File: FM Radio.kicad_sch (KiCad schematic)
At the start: 39 parts, among them IC1 SI4831-B30-GUR, J2 Conn_01x02_Pin, J4 CONSMA020.062-G, J6 CONSMA020.062-G, SW1 SW_SPDT, SW2 SW_DIP_x01, SW3 SW_Push, SW4 SW_Push, U3 LM1117MP-3.3, Y1 ECS-.327-12.5-34B-TR

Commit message: Add comments and fix errors
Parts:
- removed SW3, SW4: SW_Push, FM Radio:D6R40F1LFS, symbol Switch:SW_Push
- added S1, S2: D6R50F1LFS, D6R40F1LFS, symbol D6R50F1LFS:D6R50F1LFS
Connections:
- net GND: now also L1.1, S1.3 (NO_1), S1.4 (NO_2), S2.3 (NO_1), S2.4 (NO_2)
- net at IC1.17 (VOL-/BASS), R9.2: now also S1.1 (COM_1), S1.2 (COM_2)
- net at IC1.16 (VOL+/TREBLE), R10.2: now also S2.1 (COM_1), S2.2 (COM_2)
- net at IC1.8 (FMI), L1.2: now also C16.1
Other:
- moved on the sheet: C16, C8, C9, D3, L1, R11, U3

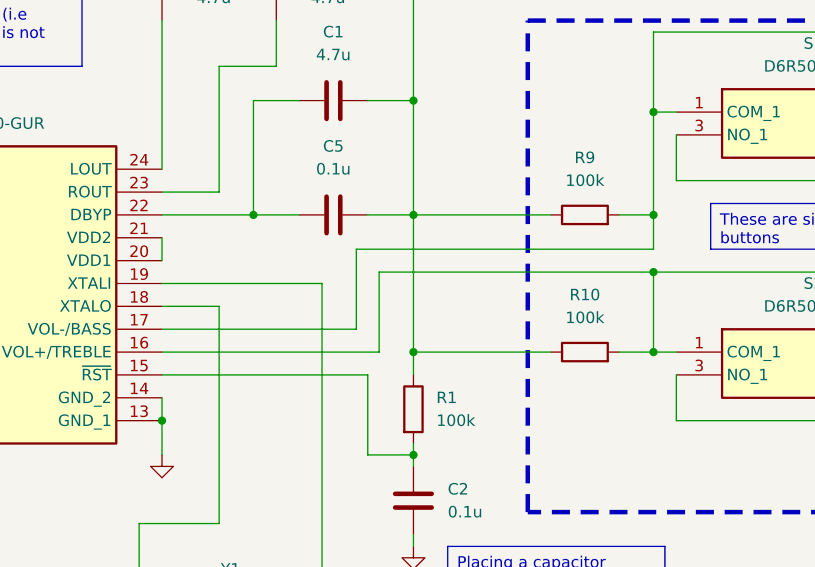
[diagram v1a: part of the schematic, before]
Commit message: Fix: VDD not connected
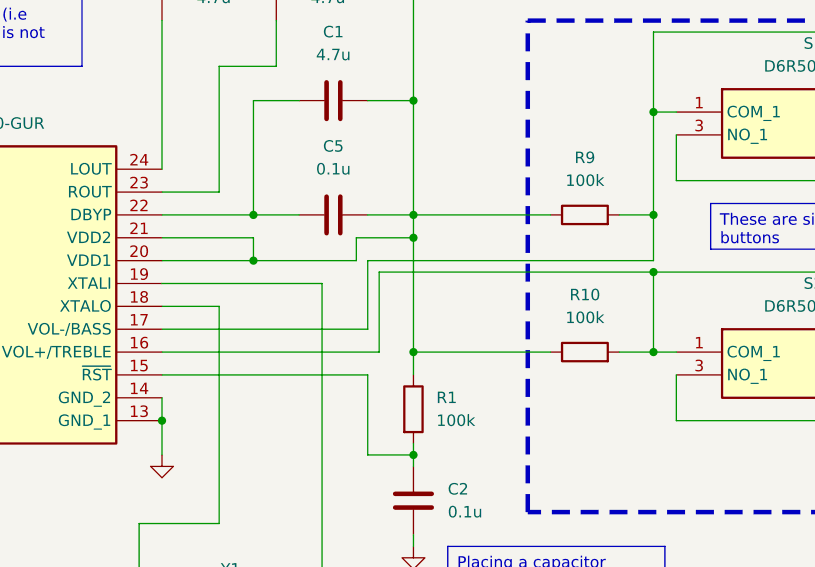
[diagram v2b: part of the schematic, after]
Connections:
- net +3.3V: now also IC1.20 (VDD1), IC1.21 (VDD2)
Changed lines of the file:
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@@
 (kicad_sch (version 20230121) (generator eeschema)
   (paper "A4")
+  (junction (at 215.9 99.06) (diameter 0) (color 0 0 0 0)
+  )
   (junction (at 57.15 156.21) (diameter 0) (color 0 0 0 0)
   )
@@
   (junction (at 138.43 91.44) (diameter 0) (color 0 0 0 0)
   )
+  (junction (at 242.57 102.87) (diameter 0) (color 0 0 0 0)
+  )
   (junction (at 275.59 92.71) (diameter 0) (color 0 0 0 0)
   )
@@
   (junction (at 242.57 85.09) (diameter 0) (color 0 0 0 0)
   )
-  (junction (at 242.57 102.87) (diameter 0) (color 0 0 0 0)
-  )
   (junction (at 36.83 167.64) (diameter 0) (color 0 0 0 0)
   )
   (junction (at 242.57 111.76) (diameter 0) (color 0 0 0 0)
+  )
+  (junction (at 198.12 101.6) (diameter 0) (color 0 0 0 0)
   )
   (junction (at 215.9 111.76) (diameter 0) (color 0 0 0 0)
@@
     (stroke (width 0) (type default))
   )
+  (wire (pts (xy 215.9 99.06) (xy 215.9 111.76))
+    (stroke (width 0) (type default))
+  )
   (wire (pts (xy 242.57 76.2) (xy 242.57 85.09))
     (stroke (width 0) (type default))
@@
     (stroke (width 0) (type default))
   )
+  (wire (pts (xy 198.12 99.06) (xy 198.12 101.6))
+    (stroke (width 0) (type default))
+  )
   (wire (pts (xy 36.83 156.21) (xy 36.83 167.64))
     (stroke (width 0) (type default))
   )
+  (wire (pts (xy 209.55 99.06) (xy 215.9 99.06))
+    (stroke (width 0) (type default))
+  )
   (wire (pts (xy 215.9 111.76) (xy 231.14 111.76))
     (stroke (width 0) (type default))
   )
+  (wire (pts (xy 242.57 102.87) (xy 242.57 111.76))
+    (stroke (width 0) (type default))
+  )
   (wire (pts (xy 187.96 104.14) (xy 205.74 104.14))
     (stroke (width 0) (type default))
@@
     (stroke (width 0) (type default))
   )
+  (wire (pts (xy 187.96 99.06) (xy 198.12 99.06))
+    (stroke (width 0) (type default))
+  )
   (wire (pts (xy 59.69 156.21) (xy 57.15 156.21))
     (stroke (width 0) (type default))
   )
-  (wire (pts (xy 187.96 109.22) (xy 209.55 109.22))
+  (wire (pts (xy 187.96 109.22) (xy 210.82 109.22))
     (stroke (width 0) (type default))
   )
@@
     (stroke (width 0) (type default))
   )
+  (wire (pts (xy 198.12 101.6) (xy 209.55 101.6))
+    (stroke (width 0) (type default))
+  )
   (wire (pts (xy 194.31 93.98) (xy 194.31 80.01))
     (stroke (width 0) (type default))
@@
     (stroke (width 0) (type default))
   )
+  (wire (pts (xy 209.55 101.6) (xy 209.55 99.06))
+    (stroke (width 0) (type default))
+  )
   (wire (pts (xy 245.11 41.91) (xy 245.11 40.64))
     (stroke (width 0) (type default))
@@
     (stroke (width 0) (type default))
   )
+  (wire (pts (xy 187.96 101.6) (xy 198.12 101.6))
+    (stroke (width 0) (type default))
+  )
   (wire (pts (xy 187.96 106.68) (xy 194.31 106.68))
     (stroke (width 0) (type default))
@@
     (stroke (width 0) (type default))
   )
-  (wire (pts (xy 215.9 96.52) (xy 215.9 111.76))
-    (stroke (width 0) (type default))
-  )
   (wire (pts (xy 185.42 130.81) (xy 185.42 144.78))
     (stroke (width 0) (type default))
@@
     (stroke (width 0) (type default))
   )
-  (wire (pts (xy 242.57 100.33) (xy 242.57 96.52))
+  (wire (pts (xy 242.57 101.6) (xy 242.57 96.52))
     (stroke (width 0) (type default))
   )
@@
     (stroke (width 0) (type default))
   )
-  (wire (pts (xy 187.96 99.06) (xy 187.96 101.6))
-    (stroke (width 0) (type default))
-  )
   (wire (pts (xy 24.13 179.07) (xy 24.13 182.88))
     (stroke (width 0) (type default))
@@
     (stroke (width 0) (type default))
   )
-  (wire (pts (xy 209.55 109.22) (xy 209.55 100.33))
+  (wire (pts (xy 210.82 109.22) (xy 210.82 101.6))
     (stroke (width 0) (type default))
   )
@@
     (stroke (width 0) (type default))
   )
-  (wire (pts (xy 209.55 100.33) (xy 242.57 100.33))
+  (wire (pts (xy 210.82 101.6) (xy 242.57 101.6))
     (stroke (width 0) (type default))
   )
@@
     (stroke (width 0) (type default))
   )
+  (wire (pts (xy 215.9 96.52) (xy 215.9 99.06))
+    (stroke (width 0) (type default))
+  )
   (wire (pts (xy 203.2 83.82) (xy 198.12 83.82))
     (stroke (width 0) (type default))
@@
     (stroke (width 0) (type default))
   )
-  (wire (pts (xy 242.57 102.87) (xy 242.57 111.76))
-    (stroke (width 0) (type default))
-  )

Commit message: Complete layout
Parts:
- R1, R10, R11, R2, R3, R4, R5, R9: footprint FM Radio:RESC1608X55N -> Resistor_SMD:R_0603_1608Metric
- S1, S2: footprint D6R40F1LFS -> FM Radio:D6R40F1LFS
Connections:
- net FM_ANT: now reaches C16.2, D4.1 (CH1), J6.1
- net AM_ANT: now reaches C17.2, D5.1 (CH1), J4.1
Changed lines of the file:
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@@
     (effects (font (size 1.27 1.27)) (justify left bottom))
   )
+  (label "AM_ANT" (at 92.71 162.56 0) (fields_autoplaced)
+    (effects (font (size 1.27 1.27)) (justify left bottom))
+  )
+  (label "FM_ANT" (at 36.83 162.56 0) (fields_autoplaced)
+    (effects (font (size 1.27 1.27)) (justify left bottom))
+  )
   (symbol (lib_id "power:GND") (at 275.59 95.25 0) (unit 1)
     (in_bom yes) (on_board yes) (dnp no) (fields_autoplaced)
@@
       (effects (font (size 1.27 1.27)))
     )
-    (property "Footprint" "D6R40F1LFS" (at 271.78 180.01 0)
+    (property "Footprint" "FM Radio:D6R40F1LFS" (at 271.78 180.01 0)
       (effects (font (size 1.27 1.27)) (justify left top) hide)
     )
@@
       (effects (font (size 1.27 1.27)) (justify left))
     )
-    (property "Footprint" "FM Radio:RESC1608X55N" (at 79.502 52.07 90)
+    (property "Footprint" "Resistor_SMD:R_0603_1608Metric" (at 79.502 52.07 90)
       (effects (font (size 1.27 1.27)) hide)
     )
@@
       (effects (font (size 1.27 1.27)))
     )
-    (property "Footprint" "FM Radio:RESC1608X55N" (at 234.95 98.298 90)
+    (property "Footprint" "Resistor_SMD:R_0603_1608Metric" (at 234.95 98.298 90)
       (effects (font (size 1.27 1.27)) hide)
     )
@@
       (effects (font (size 1.27 1.27)) (justify left))
     )
-    (property "Footprint" "FM Radio:RESC1608X55N" (at 74.422 91.44 90)
+    (property "Footprint" "Resistor_SMD:R_0603_1608Metric" (at 74.422 91.44 90)
       (effects (font (size 1.27 1.27)) hide)
     )
@@
       (effects (font (size 1.27 1.27)))
     )
-    (property "Footprint" "D6R40F1LFS" (at 271.78 206.68 0)
+    (property "Footprint" "FM Radio:D6R40F1LFS" (at 271.78 206.68 0)
       (effects (font (size 1.27 1.27)) (justify left top) hide)
     )
@@
       (effects (font (size 1.27 1.27)) (justify left))
     )
-    (property "Footprint" "FM Radio:RESC1608X55N" (at 74.422 116.84 90)
+    (property "Footprint" "Resistor_SMD:R_0603_1608Metric" (at 74.422 116.84 90)
       (effects (font (size 1.27 1.27)) hide)
     )
@@
       (effects (font (size 1.27 1.27)) (justify left))
     )
-    (property "Footprint" "FM Radio:RESC1608X55N" (at 74.422 127 90)
+    (property "Footprint" "Resistor_SMD:R_0603_1608Metric" (at 74.422 127 90)
       (effects (font (size 1.27 1.27)) hide)
     )
@@
       (effects (font (size 1.27 1.27)) (justify left))
     )
-    (property "Footprint" "FM Radio:RESC1608X55N" (at 214.122 118.11 90)
+    (property "Footprint" "Resistor_SMD:R_0603_1608Metric" (at 214.122 118.11 90)
       (effects (font (size 1.27 1.27)) hide)
     )
@@
       (effects (font (size 1.27 1.27)))
     )
-    (property "Footprint" "FM Radio:RESC1608X55N" (at 234.95 113.538 90)
+    (property "Footprint" "Resistor_SMD:R_0603_1608Metric" (at 234.95 113.538 90)
       (effects (font (size 1.27 1.27)) hide)
     )
@@
       (effects (font (size 1.27 1.27)) (justify left))
     )
-    (property "Footprint" "FM Radio:RESC1608X55N" (at 74.422 104.14 90)
-      (effects (font (size 1.27 1.27)) hide)
-    )
+    (property "Footprint" "Resistor_SMD:R_0603_1608Metric" (at 74.422 104.14 90)
+      (effects (font (size 1.27 1.27)) hide)
+    )
